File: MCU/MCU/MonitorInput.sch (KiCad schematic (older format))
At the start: 61 parts, among them J10 Conn_01x02, J5 Conn_01x04, J6 Conn_01x02, J7 Conn_01x02, J8 Conn_01x06, J9 Conn_01x06, U3 LMV324, U4 LMV324, U5 LMV358, U6 LMV324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

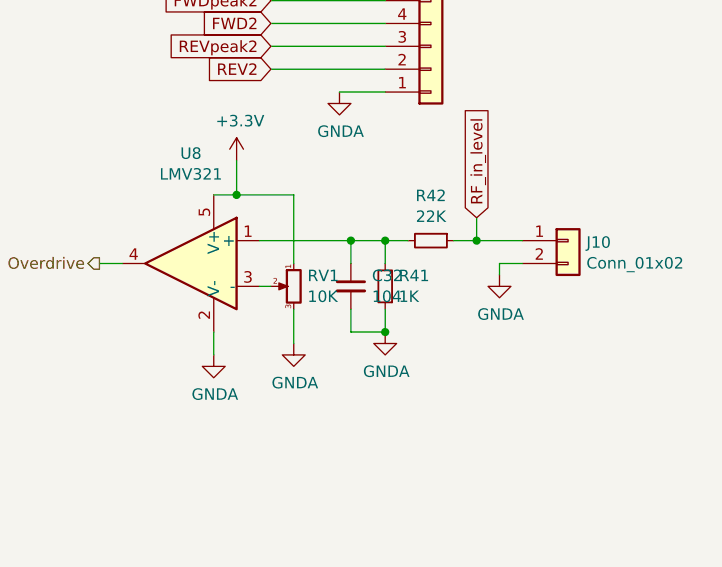
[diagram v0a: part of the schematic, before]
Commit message: OPA1000 and 2000 compatibility
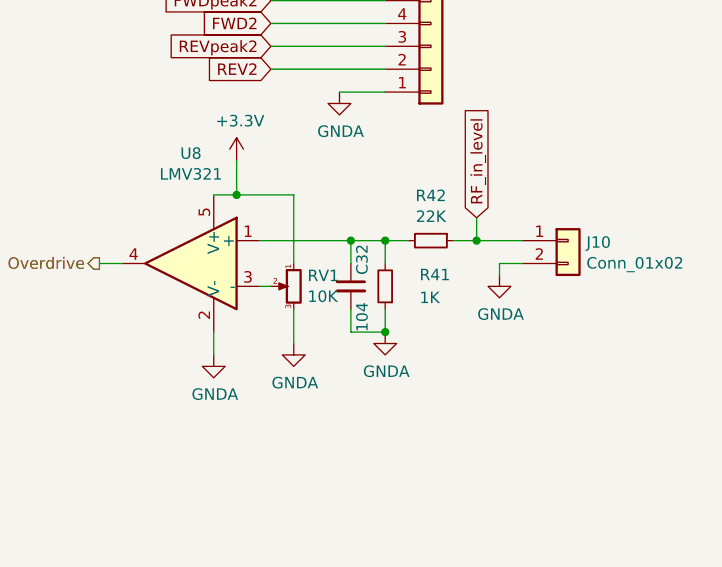
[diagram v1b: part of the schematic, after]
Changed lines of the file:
@@
 EESchema Schematic File Version 4
-LIBS:MCU-cache
 EELAYER 30 0
 EELAYER END
@@
 U 1 1 5F433A00
 P 9400 5750
-F 0 "R41" H 9341 5704 50  0000 R CNN
-F 1 "1K" H 9341 5795 50  0000 R CNN
+F 0 "R41" H 9250 5700 50  0000 R CNN
+F 1 "1K" H 9250 5800 50  0000 R CNN
 F 2 "Resistors_SMD:R_0805" H 9400 5750 50  0001 C CNN
 F 3 "~" H 9400 5750 50  0001 C CNN
@@
 U 1 1 5F4C3B98
 P 9250 5750
-F 0 "C32" H 9342 5796 50  0000 L CNN
-F 1 "104" H 9342 5705 50  0000 L CNN
+F 0 "C32" V 9300 5800 50  0000 L CNN
+F 1 "104" V 9300 5550 50  0000 L CNN
 F 2 "Capacitors_SMD:C_0805" H 9250 5750 50  0001 C CNN
 F 3 "~" H 9250 5750 50  0001 C CNN
